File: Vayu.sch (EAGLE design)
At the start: 63 parts, among them J1 1770911, J2 1770911, J3 3220-10-0100-00, J4 SM04B-SRSS-TB(LF)(SN), Q1 IRLML6402TRPBF, Q2 IRLML6402TRPBF, Q3 IRLML6402TRPBF, Q4 IRLML6402TRPBF, SW1 TL1105LF160Q, SW2 TL1105LF160Q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

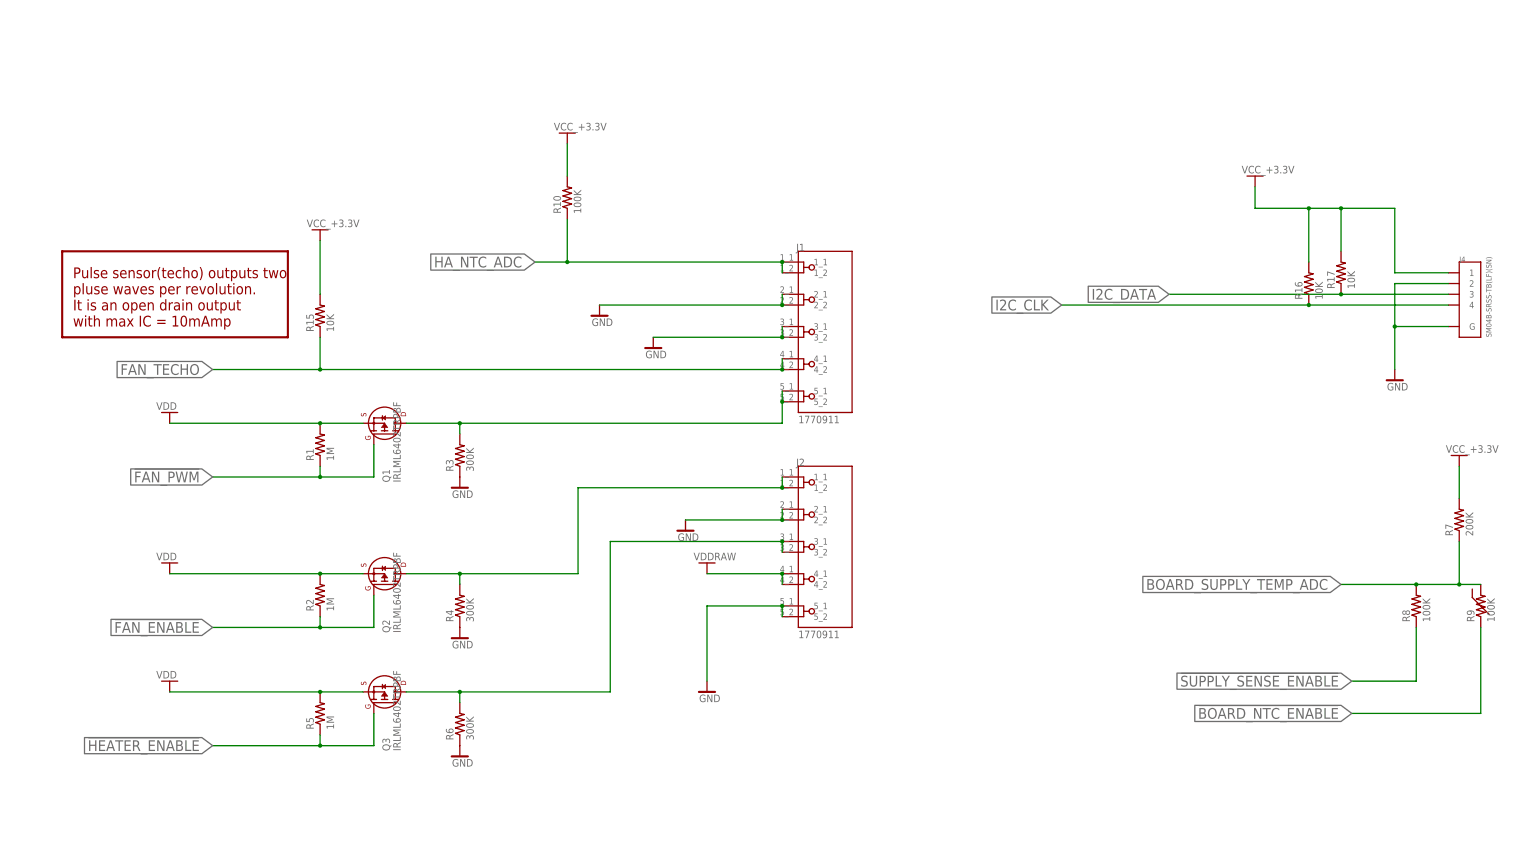
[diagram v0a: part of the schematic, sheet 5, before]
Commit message: removed sch bugs and WIP in brd
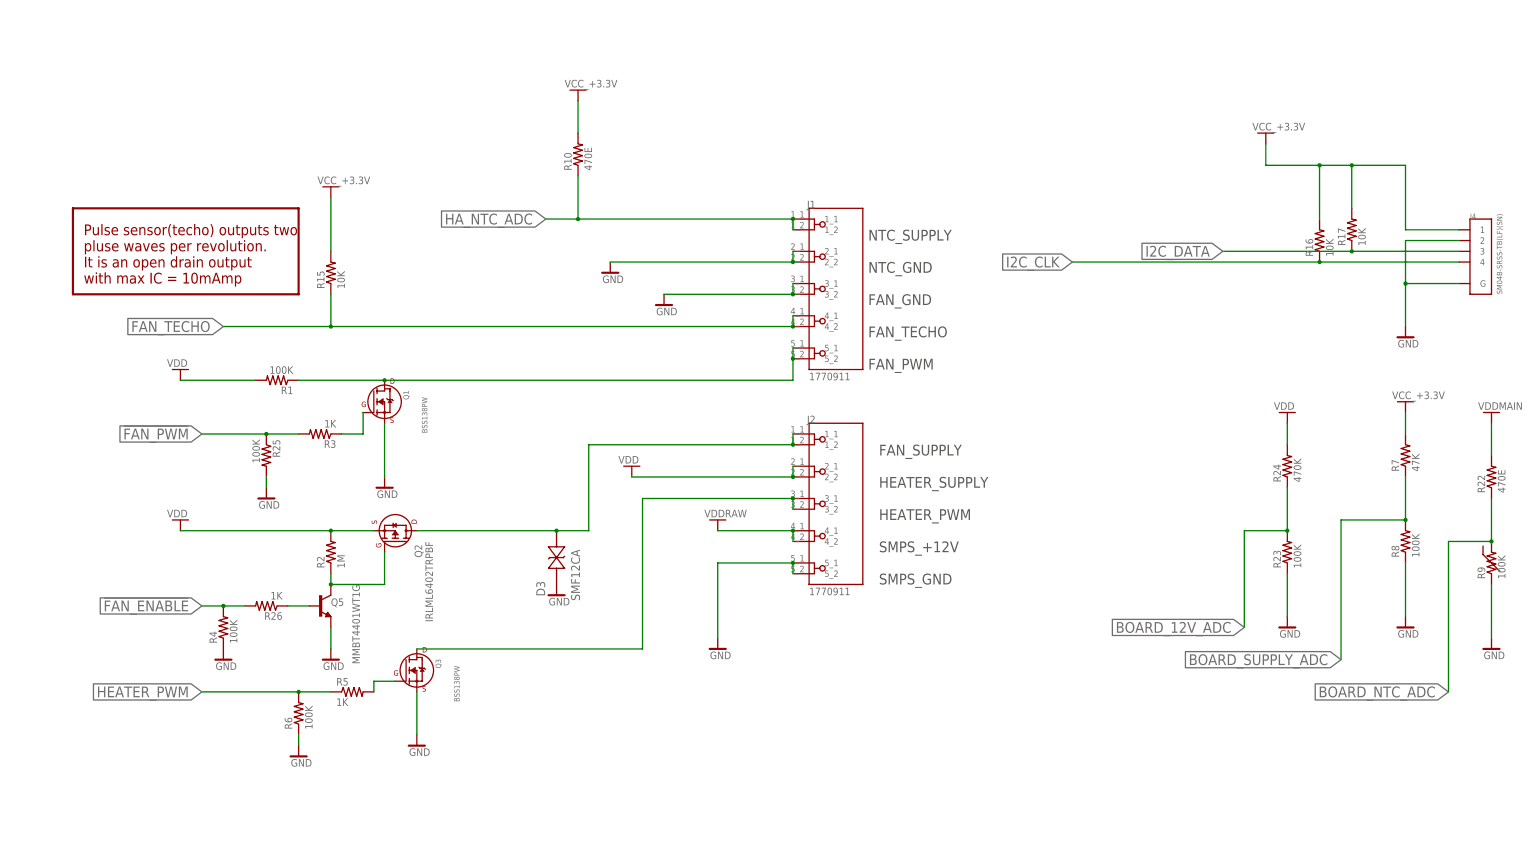
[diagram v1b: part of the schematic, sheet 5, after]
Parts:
- added C13, C14: 1nF, rcl:C-EUC0402S
- added D3: SMF12CA, diodes:SMF12CA
- added Q5: MMBT4401WT1G, transistors-BJT:MMBT4401WT1G
- added R22: 470E, rcl:R-US_R0402
- added R23, R25: 100K, rcl:R-US_R0402
- added R24: 470K, rcl:R-US_R0402
- added R26: 1K, rcl:R-US_R0402
- Q1, Q3: value IRLML6402TRPBF -> BSS138PW; device mosfets:IRLML6402TRPBF -> mosfets:BSS138PW
- R1: value 1M -> 100K
- R10: value 100K -> 470E
- R3: value 300K -> 1K
- R4, R6: value 300K -> 100K
- R5: value 1M -> 1K
- R7: value 200K -> 47K
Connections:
- removed net !BOARD_NTC_ENABLE: R9.1, U1.P5-PD14-EM4WU
- removed net !HEATER_ENABLE: Q3.G, R5.1, U1.P9-PD10(5V)
- removed net !SUPPLY_SENSE_ENABLE: R8.1, U1.P4-PD15
- removed net BOARD_SUPPLY_TEMP_ADC: C2.1, R7.1, R8.2, R9.2, U1.P6-PD13
- new net BOARD_12V_ADC: C13.1, R23.2, R24.1, U1.P4-PD15
- new net BOARD_NTC_ADC: C14.1, R22.1, R9.2, U1.P5-PD14-EM4WU
- new net BOARD_SUPPLY_ADC: C2.1, R7.1, R8.2, U1.P6-PD13
- new net HEATER_PWM: R5.1, R6.2, U1.P9-PD10(5V)
- new net N$1: Q1.G, R3.1
- new net N$2: Q3.G, R5.2
- new net N$5: Q5.B, R26.1
- new net PMOSFET_EN: Q2.G, Q5.C, R2.1
- net !FAN_ENABLE: now also R26.2, R4.2; no longer Q2.G, R2.1
- net !FAN_PWM: now also R25.1, R3.2; no longer Q1.G, R1.1
- net FAN_SPEED: now also R1.1; no longer R3.2
- net FAN_SUPPLY: now also D3.11; no longer R4.2
- net GND: now also C13.2, C14.2, D3.12, Q1.S, Q3.S, Q5.E, R23.1, R25.2, R8.1, R9.1; no longer J2.2_1, J2.2_2, R3.1
- net HEATER: no longer R6.2
- net VDD: now also J2.2_1, J2.2_2, R24.2; no longer Q1.S, Q3.S, R5.2
- net VDDMAIN: now also R22.2
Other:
- note added: "FAN_SUPPLY HEATER_SUPPLY HEATER_PWM SMPS_+12V SMPS_GND"
- note added: "NTC_SUPPLY NTC_GND FAN_GND FAN_TECHO FAN_PWM"
- moved on the sheet: C2, C7, C8, J1, J2, J4, Q2, R1, R10, R12, R13, R15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

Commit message: bug fix, updated MOSFET driver and other MOSFETS, added SWO support
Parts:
- Q3: value BSS138PW -> DMN2056U; device mosfets:BSS138PW -> mosfets:DMN2056U
- R10, R22: value 470E -> 200K
- R23: value 100K -> 10K
- R24: value 470K -> 47K
- R26, R3, R5: value 1K -> 10K
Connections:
- removed net SERIAL_CTS: TP8.TP, U1.(5V)I2C1-PC11-P26
- removed net SERIAL_RTS: TP9.TP, U1.(5V)PC6-P24
- new net JTAG_SWO: J3.6, TP8.TP, U1.(5V)I2C1-PC11-P26
- net GND: now also TP9.TP
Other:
- note added: "BOARD NTC calculations Vref = VDDMAIN = 3.0 V Beta = 4250 Temp Res Kohm mVolt -20 1260.25 2848 120 3.192 52"
- note added: "HA NTC calculations Vref = VDDMAIN = 3.0 V Beta = 3950 Temp Res Kohm mVolt -20 1053.846 2774 120 4.070 66"
- moved on the sheet: TP9
